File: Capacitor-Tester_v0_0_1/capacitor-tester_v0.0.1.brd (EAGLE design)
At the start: 100 x 80 mm, 32 parts, among them IC1 AD8531ARZ, IC2 MC34063EBD-TR, IC3 DAC6571IDBVT, IC4 AD8531ARZ, J1 USB4125-GF-A-0190_REVA2, J2 DS1044-140G, J4 250-103, U1 AD5933, U2 LM6171AIMX/NOPB, Y1 LFSPXO018034

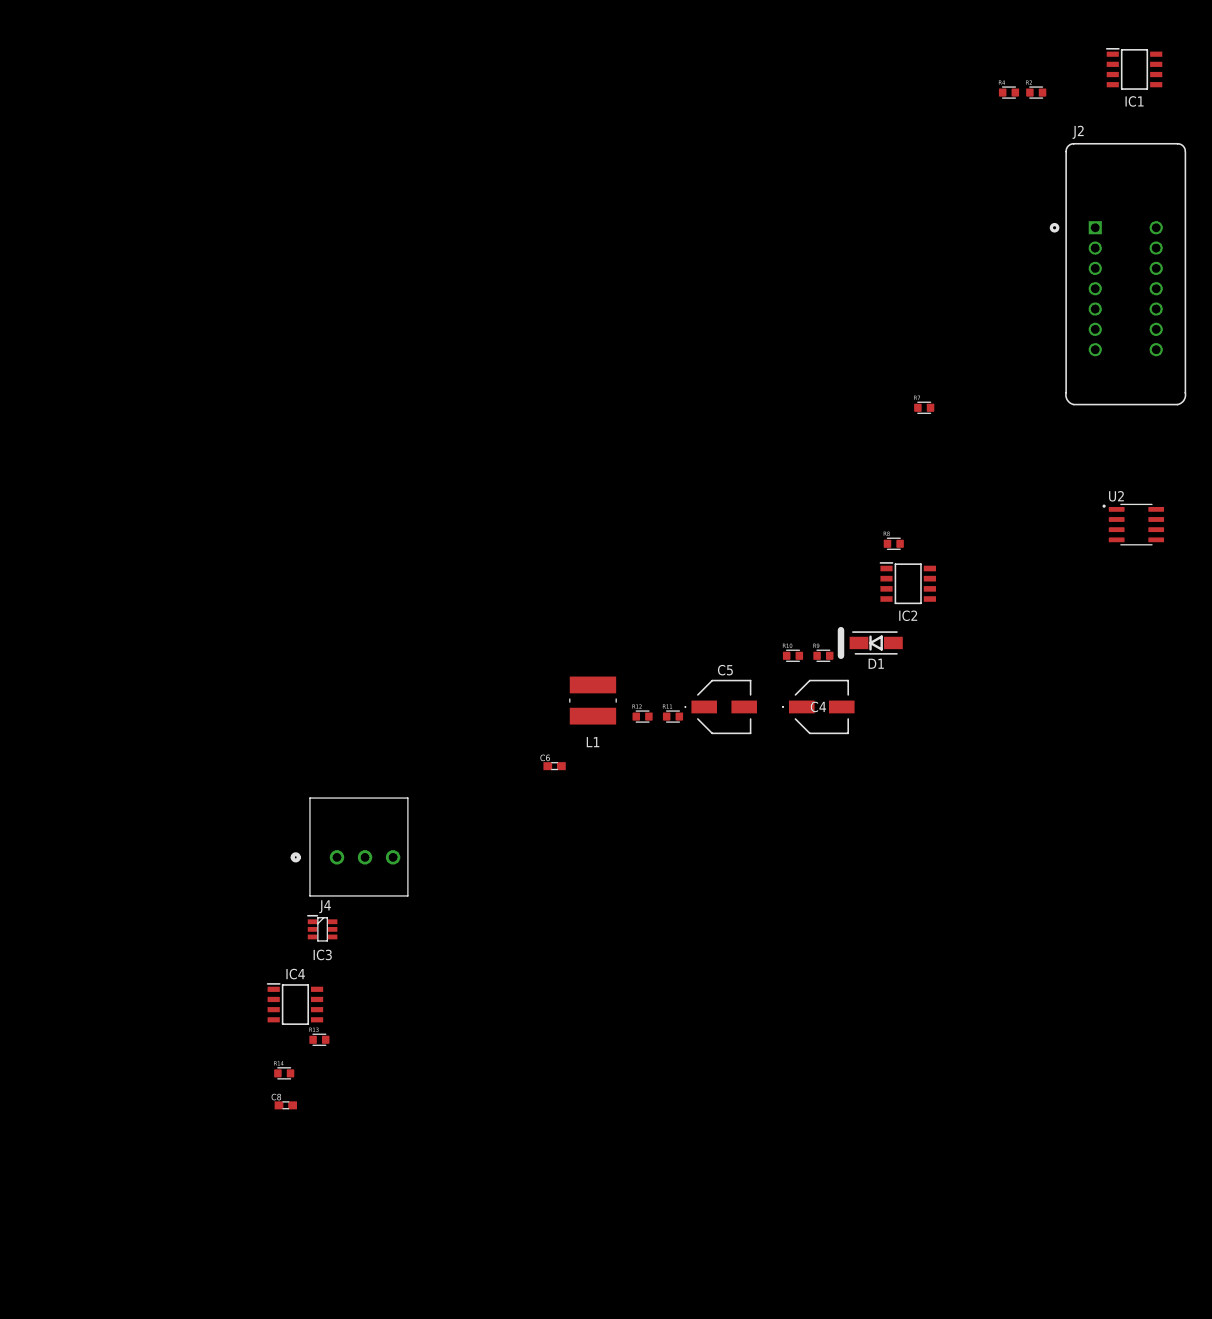
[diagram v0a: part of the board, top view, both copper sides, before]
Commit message: v0.0.1 - Changed both stages of the opamps. Need to change from 15V to 12V
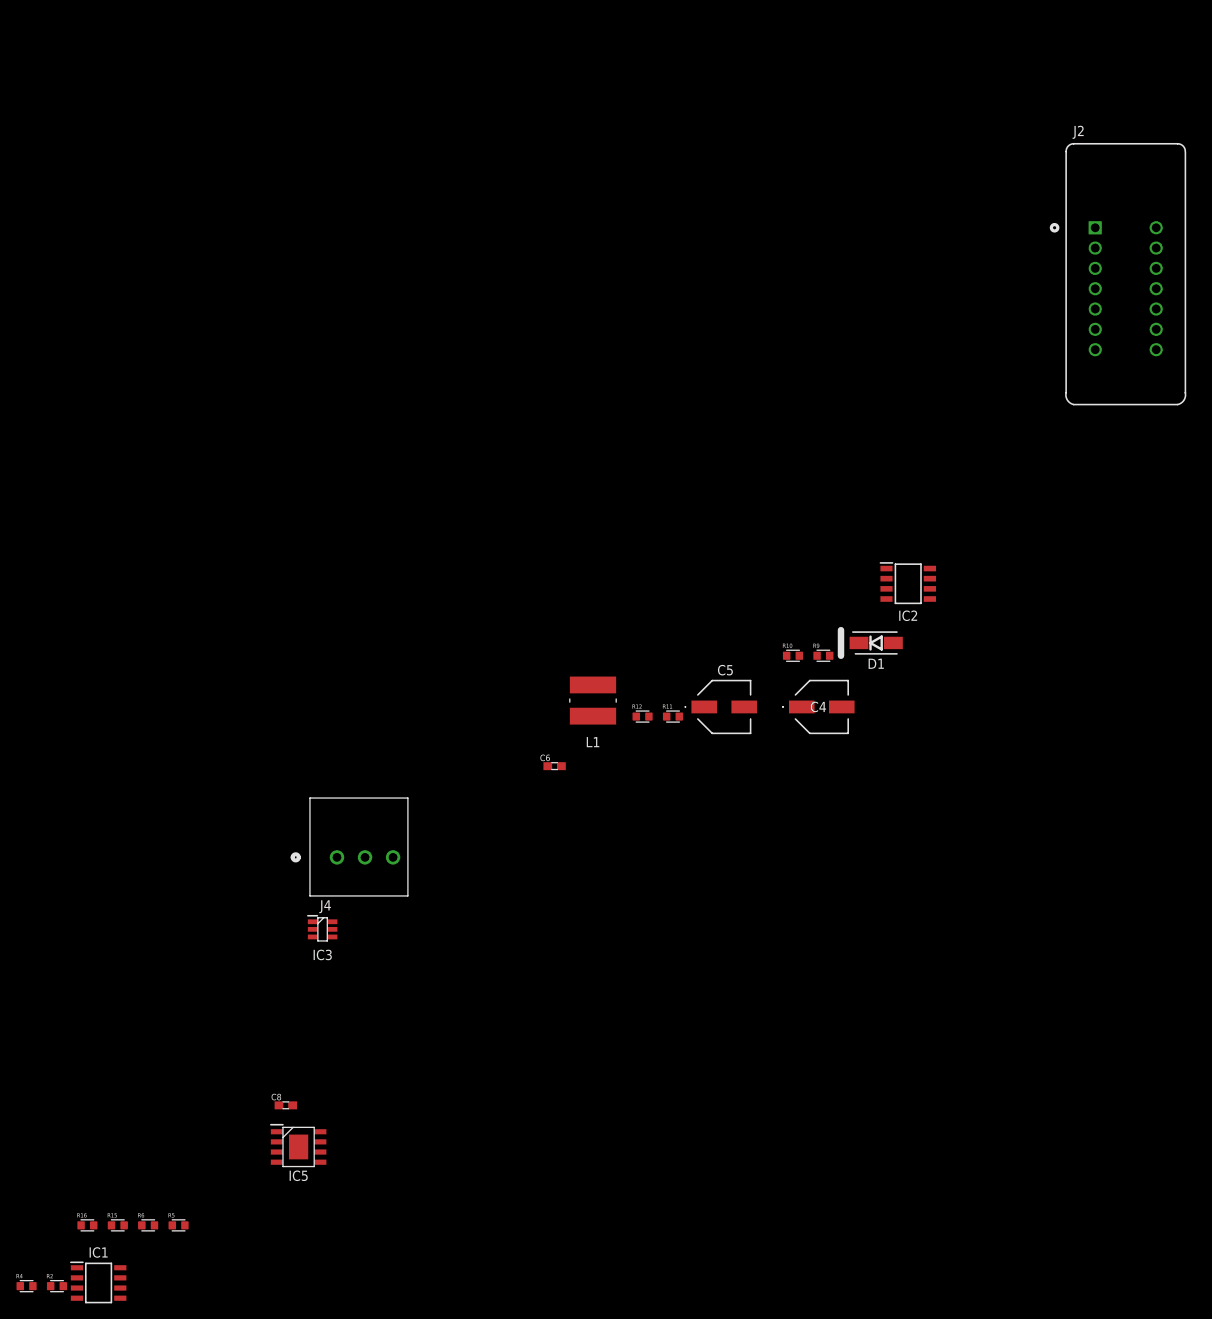
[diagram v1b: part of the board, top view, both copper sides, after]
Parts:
- removed IC4: AD8531ARZ, AD8531ARZ:SOIC127P600X175-8N
- removed R13: 5k-1%, custom_library:R0603
- removed R14, R8: 10k-1%, custom_library:R0603
- removed R7: DNP-100R-1%, custom_library:R0603
- removed U2: LM6171AIMX/NOPB, LM6171AIMX_NOPB:SOIC127P599X175-8N
- added IC5: AD8397ARDZ, AD8397ARDZ:SOIC127P600X175-9N
- added R15: 5k-1%, custom_library:R0603
- added R16, R5: 10k-1%, custom_library:R0603
- added R6: 1k-1%, custom_library:R0603
- R4: value 1k-1% -> DNP-10k-1%
- moved IC1 199.4 mm to (-132.2, -260.0)
- moved R4 193.2 mm to (-141.2, -260.4)
- moved R2 193.0 mm to (-137.4, -260.4)
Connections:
- removed net N$2: R8.2, U2.2
- removed net N$3: R8.1, U2.6
- removed net N$9: IC4.2, R13.1, R14.1
- new net N$12: IC5.8
- new net N$13: IC5.6, R15.1, R16.2
- new net N$4: IC5.2, R5.1, R6.1
- new net Z_OUT: IC1.2, J2.10, J2.11, J2.12, J2.13, J2.14, J2.8, J2.9, R2.2
- net +15V: no longer U2.7
- net +5V: no longer IC4.7
- net DAC_OUT: now also IC5.5; no longer IC4.3
- net GND: now also IC1.3, IC5.4, IC5.9, R15.2; no longer IC4.4, R13.2, U2.3, U2.4
- net N$1: now also IC1.6, R4.2; no longer IC1.2, R4.1
- net RFB: no longer R7.2
- net UZA_OUT: now also IC5.1, R6.2; no longer IC1.6, R4.2
- net UZB_OUT: now also IC5.3, IC5.7, R16.1; no longer IC1.3, IC4.6, R14.2
- net VIN: now also R4.1; no longer J2.10, J2.11, J2.12, J2.13, J2.14, J2.8, J2.9, R7.1
- net VOUT: now also R5.2; no longer R2.2

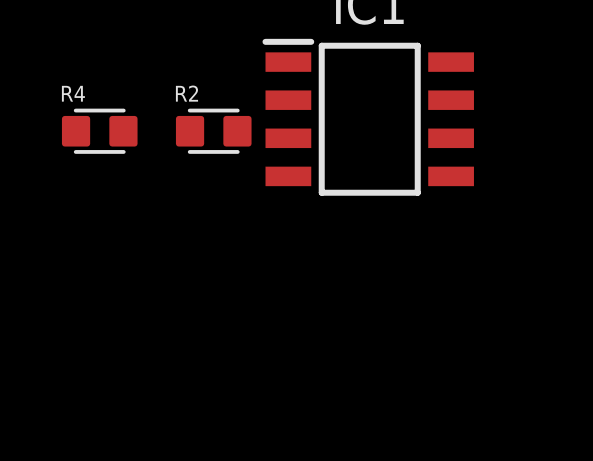
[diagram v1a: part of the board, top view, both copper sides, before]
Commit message: v0.0.1 - Changed boost converter to +12V on output and added shottky diode
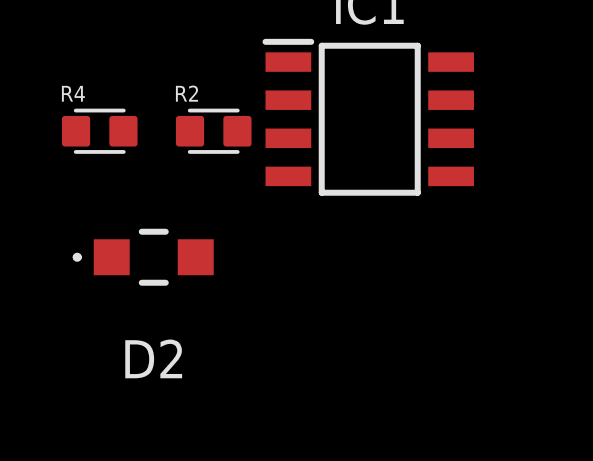
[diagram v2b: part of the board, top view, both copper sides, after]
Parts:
- added D2: PMEG6020ER,115, PMEG6020ER_115:PMEG6020ER115
- C4: value EEEFKC271XSP -> 270u / 16V
- C5: value VS1C101ME054000CE0 -> 270u / 16V
- L1: value SDR0604-221KL -> 220u
- R10: value 910R-1% -> 1k-1%
- R11: value 0603WAJ022KT5E -> R270-1%
- R9: value 10k-1% -> 8k66-1%
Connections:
- removed net +15V: C4.1, D1.1, R9.1
- removed net N$12: IC5.8
- new net +12V: C4.1, D1.1, D2.1, IC5.8, R9.1
- net Z_OUT: now also D2.2
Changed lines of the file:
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@@
 <attribute name="VALUE" x="-35" y="-180" size="1.27" layer="27" align="center"/>
 </element>
-<element name="R9" library="custom_library" package="R0603" value="10k-1%" x="-41.6" y="-181.6" smashed="yes">
+<element name="R9" library="custom_library" package="R0603" value="8k66-1%" x="-41.6" y="-181.6" smashed="yes">
 <attribute name="NAME" x="-42.92476875" y="-180.613721875" size="0.52744375" layer="25"/>
 <attribute name="VALUE" x="-43.319259375" y="-183.12958125" size="0.525771875" layer="27"/>
 </element>
-<element name="R10" library="custom_library" package="R0603" value="910R-1%" x="-45.4" y="-181.6" smashed="yes">
+<element name="R10" library="custom_library" package="R0603" value="1k-1%" x="-45.4" y="-181.6" smashed="yes">
 <attribute name="NAME" x="-46.72476875" y="-180.613721875" size="0.52744375" layer="25"/>
 <attribute name="VALUE" x="-47.119259375" y="-183.12958125" size="0.525771875" layer="27"/>
 </element>
-<element name="C4" library="EEEFKC271XSP" package="EEE0JA331XP" value="EEEFKC271XSP" x="-41.8" y="-188" smashed="yes">
+<element name="C4" library="EEEFKC271XSP" package="EEE0JA331XP" value="270u / 16V" x="-41.8" y="-188" smashed="yes">
 <attribute name="DESCRIPTION" value="Panasonic 270uF 16 V dc Aluminium Electrolytic Capacitor, FKS Series 2000h 6.3 (Dia.) x 7.7mm" x="-41.8" y="-188" size="1.778" layer="27" display="off"/>
 <attribute name="HEIGHT" value="7.8mm" x="-41.8" y="-188" size="1.778" layer="27" display="off"/>
@@
 <attribute name="VALUE" x="-42.225" y="-188" size="1.27" layer="27" align="center"/>
 </element>
-<element name="C5" library="EEEFKC271XSP" package="EEE0JA331XP" value="VS1C101ME054000CE0" x="-54" y="-188" smashed="yes">
+<element name="C5" library="EEEFKC271XSP" package="EEE0JA331XP" value="270u / 16V" x="-54" y="-188" smashed="yes">
 <attribute name="DESCRIPTION" value="Panasonic 270uF 16 V dc Aluminium Electrolytic Capacitor, FKS Series 2000h 6.3 (Dia.) x 7.7mm" x="-54" y="-188" size="1.778" layer="27" display="off"/>
 <attribute name="HEIGHT" value="7.8mm" x="-54" y="-188" size="1.778" layer="27" display="off"/>
@@
 <attribute name="TME_ELECTRONIC_COMPONENTS_PRICE-STOCK" value="" x="-54" y="-188" size="1.778" layer="27" display="off"/>
 </element>
-<element name="R11" library="custom_library" package="R0603" value="0603WAJ022KT5E" x="-60.4" y="-189.2" smashed="yes">
+<element name="R11" library="custom_library" package="R0603" value="R270-1%" x="-60.4" y="-189.2" smashed="yes">
 <attribute name="NAME" x="-61.72476875" y="-188.213721875" size="0.52744375" layer="25"/>
 <attribute name="VALUE" x="-62.119259375" y="-190.72958125" size="0.525771875" layer="27"/>
@@
 <attribute name="VALUE" x="-65.919259375" y="-190.72958125" size="0.525771875" layer="27"/>
 </element>
-<element name="L1" library="SDR0604-221KL" package="SDR0604221KL" value="SDR0604-221KL" x="-70.4" y="-187.2" smashed="yes">
+<element name="L1" library="SDR0604-221KL" package="SDR0604221KL" value="220u" x="-70.4" y="-187.2" smashed="yes">
 <attribute name="DESCRIPTION" value="Fixed Inductors 220uH 10% SMD 0604" x="-70.4" y="-187.2" size="1.778" layer="27" display="off"/>
 <attribute name="HEIGHT" value="4.8mm" x="-70.4" y="-187.2" size="1.778" layer="27" display="off"/>
@@
 <attribute name="NAME" x="-142.52476875" y="-259.413721875" size="0.52744375" layer="25"/>
 <attribute name="VALUE" x="-142.919259375" y="-261.92958125" size="0.525771875" layer="27"/>
+</element>
+<element name="D2" library="PMEG6020ER_115" package="PMEG6020ER115" value="PMEG6020ER,115" x="-139.4" y="-264.6" smashed="yes">
+<attribute name="DESCRIPTION" value="Nexperia PMEG6020ER,115 SMT Schottky Diode, 60V 2A, 2-Pin SOD-123W" x="-139.4" y="-264.6" size="1.778" layer="27" display="off"/>
+<attribute name="HEIGHT" value="1.1mm" x="-139.4" y="-264.6" size="1.778" layer="27" display="off"/>
+<attribute name="MANUFACTURER_NAME" value="Nexperia" x="-139.4" y="-264.6" size="1.778" layer="27" display="off"/>
+<attribute name="MANUFACTURER_PART_NUMBER" value="PMEG6020ER,115" x="-139.4" y="-264.6" size="1.778" layer="27" display="off"/>
+<attribute name="NAME" x="-139.4" y="-268" size="1.27" layer="25" align="center"/>
+<attribute name="TME_ELECTRONIC_COMPONENTS_PART_NUMBER" value="" x="-139.4" y="-264.6" size="1.778" layer="27" display="off"/>
+<attribute name="TME_ELECTRONIC_COMPONENTS_PRICE-STOCK" value="" x="-139.4" y="-264.6" size="1.778" layer="27" display="off"/>
+<attribute name="VALUE" x="-139.4" y="-264.6" size="1.27" layer="27" align="center"/>
 </element>
 </elements>
@@
 <wire x1="-76.05" y1="-195.4" x2="-33.712" y2="-173.235" width="0" layer="19" extent="1-1"/>
 </signal>
-<signal name="+15V">
-<contactref element="D1" pad="1"/>
-<contactref element="R9" pad="1"/>
-<contactref element="C4" pad="1"/>
-<wire x1="-42.39" y1="-181.6" x2="-44.3" y2="-188" width="0" layer="19" extent="1-1"/>
-<wire x1="-37.15" y1="-180" x2="-42.39" y2="-181.6" width="0" layer="19" extent="1-1"/>
-</signal>
 <signal name="N$6">
 <contactref element="SJ1" pad="2"/>
@@
 <wire x1="-130.59" y1="-252.8" x2="-132.81" y2="-252.8" width="0" layer="19" extent="1-1"/>
 <wire x1="-104.488" y1="-243.635" x2="-130.59" y2="-252.8" width="0" layer="19" extent="1-1"/>
-</signal>
-<signal name="N$12">
-<contactref element="IC5" pad="8"/>
 </signal>
 <signal name="Z_OUT">
@@
 <contactref element="IC1" pad="2"/>
 <contactref element="R2" pad="2"/>
+<contactref element="D2" pad="2"/>
+<wire x1="-136.61" y1="-260.4" x2="-138" y2="-264.6" width="0" layer="19" extent="1-1"/>
+<wire x1="-134.912" y1="-259.365" x2="-136.61" y2="-260.4" width="0" layer="19" extent="1-1"/>
+<wire x1="0" y1="-143.34" x2="-134.912" y2="-259.365" width="0" layer="19" extent="1-1"/>
 <wire x1="0" y1="-140.8" x2="0" y2="-143.34" width="0" layer="19" extent="1-1"/>
 <wire x1="0" y1="-138.26" x2="0" y2="-140.8" width="0" layer="19" extent="1-1"/>
@@
 <wire x1="0" y1="-130.64" x2="0" y2="-133.18" width="0" layer="19" extent="1-1"/>
 <wire x1="0" y1="-128.1" x2="0" y2="-130.64" width="0" layer="19" extent="1-1"/>
-<wire x1="-134.912" y1="-259.365" x2="0" y2="-143.34" width="0" layer="19" extent="1-1"/>
-<wire x1="-136.61" y1="-260.4" x2="-134.912" y2="-259.365" width="0" layer="19" extent="1-1"/>
 </signal>
 <signal name="N$1">
@@
 <wire x1="-129.488" y1="-260.635" x2="-138.19" y2="-260.4" width="0" layer="19" extent="1-1"/>
 </signal>
+<signal name="+12V">
+<contactref element="D1" pad="1"/>
+<contactref element="R9" pad="1"/>
+<contactref element="C4" pad="1"/>
+<contactref element="IC5" pad="8"/>
+<contactref element="D2" pad="1"/>
+<wire x1="-42.39" y1="-181.6" x2="-44.3" y2="-188" width="0" layer="19" extent="1-1"/>
+<wire x1="-37.15" y1="-180" x2="-42.39" y2="-181.6" width="0" layer="19" extent="1-1"/>
+<wire x1="-104.488" y1="-241.095" x2="-44.3" y2="-188" width="0" layer="19" extent="1-1"/>
+<wire x1="-140.8" y1="-264.6" x2="-104.488" y2="-241.095" width="0" layer="19" extent="1-1"/>
+</signal>
 </signals>

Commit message: v0.0.1 - Changed L1
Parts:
- L1: value 220u -> 15uH; device SDR0604-221KL:SDR0604221KL -> SDR0604-150YL:SDR0604330KL
- R11: value R270-1% -> R133-1%
- moved L1 112.6 mm to (-143.6, -272.8)
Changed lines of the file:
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@@
 <attribute name="TME_ELECTRONIC_COMPONENTS_PRICE-STOCK" value="" x="-54" y="-188" size="1.778" layer="27" display="off"/>
 </element>
-<element name="R11" library="custom_library" package="R0603" value="R270-1%" x="-60.4" y="-189.2" smashed="yes">
+<element name="R11" library="custom_library" package="R0603" value="R133-1%" x="-60.4" y="-189.2" smashed="yes">
 <attribute name="NAME" x="-61.72476875" y="-188.213721875" size="0.52744375" layer="25"/>
 <attribute name="VALUE" x="-62.119259375" y="-190.72958125" size="0.525771875" layer="27"/>
@@
 <attribute name="NAME" x="-65.52476875" y="-188.213721875" size="0.52744375" layer="25"/>
 <attribute name="VALUE" x="-65.919259375" y="-190.72958125" size="0.525771875" layer="27"/>
-</element>
-<element name="L1" library="SDR0604-221KL" package="SDR0604221KL" value="220u" x="-70.4" y="-187.2" smashed="yes">
-<attribute name="DESCRIPTION" value="Fixed Inductors 220uH 10% SMD 0604" x="-70.4" y="-187.2" size="1.778" layer="27" display="off"/>
-<attribute name="HEIGHT" value="4.8mm" x="-70.4" y="-187.2" size="1.778" layer="27" display="off"/>
-<attribute name="MANUFACTURER_NAME" value="Bourns" x="-70.4" y="-187.2" size="1.778" layer="27" display="off"/>
-<attribute name="MANUFACTURER_PART_NUMBER" value="SDR0604-221KL" x="-70.4" y="-187.2" size="1.778" layer="27" display="off"/>
-<attribute name="NAME" x="-70.4" y="-192.4" size="1.27" layer="25" align="center"/>
-<attribute name="TME_ELECTRONIC_COMPONENTS_PART_NUMBER" value="" x="-70.4" y="-187.2" size="1.778" layer="27" display="off"/>
-<attribute name="TME_ELECTRONIC_COMPONENTS_PRICE-STOCK" value="" x="-70.4" y="-187.2" size="1.778" layer="27" display="off"/>
-<attribute name="VALUE" x="-70.4" y="-187.2" size="1.27" layer="27" align="center"/>
 </element>
 <element name="C6" library="custom_library" package="C0603" value="560p" x="-75.2" y="-195.4" smashed="yes">
@@
 <attribute name="TME_ELECTRONIC_COMPONENTS_PRICE-STOCK" value="" x="-139.4" y="-264.6" size="1.778" layer="27" display="off"/>
 <attribute name="VALUE" x="-139.4" y="-264.6" size="1.27" layer="27" align="center"/>
+</element>
+<element name="L1" library="SDR0604-150YL" package="SDR0604330KL" value="15uH" x="-143.6" y="-272.8" smashed="yes">
+<attribute name="DESCRIPTION" value="Bourns SDR0604 Series Wire-wound SMD Inductor with a Ferrite Core, 15 uH +/-15% 1.6A Idc Q:30" x="-143.6" y="-272.8" size="1.778" layer="27" display="off"/>
+<attribute name="HEIGHT" value="4.8mm" x="-143.6" y="-272.8" size="1.778" layer="27" display="off"/>
+<attribute name="MANUFACTURER_NAME" value="Bourns" x="-143.6" y="-272.8" size="1.778" layer="27" display="off"/>
+<attribute name="MANUFACTURER_PART_NUMBER" value="SDR0604-150YL" x="-143.6" y="-272.8" size="1.778" layer="27" display="off"/>
+<attribute name="NAME" x="-143.6" y="-272.8" size="1.27" layer="25" align="center"/>
+<attribute name="TME_ELECTRONIC_COMPONENTS_PART_NUMBER" value="" x="-143.6" y="-272.8" size="1.778" layer="27" display="off"/>
+<attribute name="TME_ELECTRONIC_COMPONENTS_PRICE-STOCK" value="" x="-143.6" y="-272.8" size="1.778" layer="27" display="off"/>
+<attribute name="VALUE" x="-143.6" y="-272.8" size="1.27" layer="27" align="center"/>
 </element>
 </elements>
@@
 <contactref element="D1" pad="2"/>
 <contactref element="L1" pad="2"/>
-<wire x1="-32.85" y1="-180" x2="-70.4" y2="-185.25" width="0" layer="19" extent="1-1"/>
 <wire x1="-33.712" y1="-170.695" x2="-32.85" y2="-180" width="0" layer="19" extent="1-1"/>
+<wire x1="-143.6" y1="-270.85" x2="-32.85" y2="-180" width="0" layer="19" extent="1-1"/>
 </signal>
 <signal name="N$7">
@@
 <contactref element="L1" pad="1"/>
 <wire x1="-59.61" y1="-189.2" x2="-63.41" y2="-189.2" width="0" layer="19" extent="1-1"/>
-<wire x1="-70.4" y1="-189.15" x2="-63.41" y2="-189.2" width="0" layer="19" extent="1-1"/>
 <wire x1="-28.288" y1="-171.965" x2="-59.61" y2="-189.2" width="0" layer="19" extent="1-1"/>
+<wire x1="-143.6" y1="-274.75" x2="-63.41" y2="-189.2" width="0" layer="19" extent="1-1"/>
 </signal>
 <signal name="N$8">
